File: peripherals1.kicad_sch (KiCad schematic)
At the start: 39 parts, among them Q1 Q_NMOS_GSD, SW3 SW_Push, SW4 SW_Push, SW5 SW_Push, SW6 SW_Push, SW7 SW_Push, SW8 SW_Push, U7 TSDP343xx

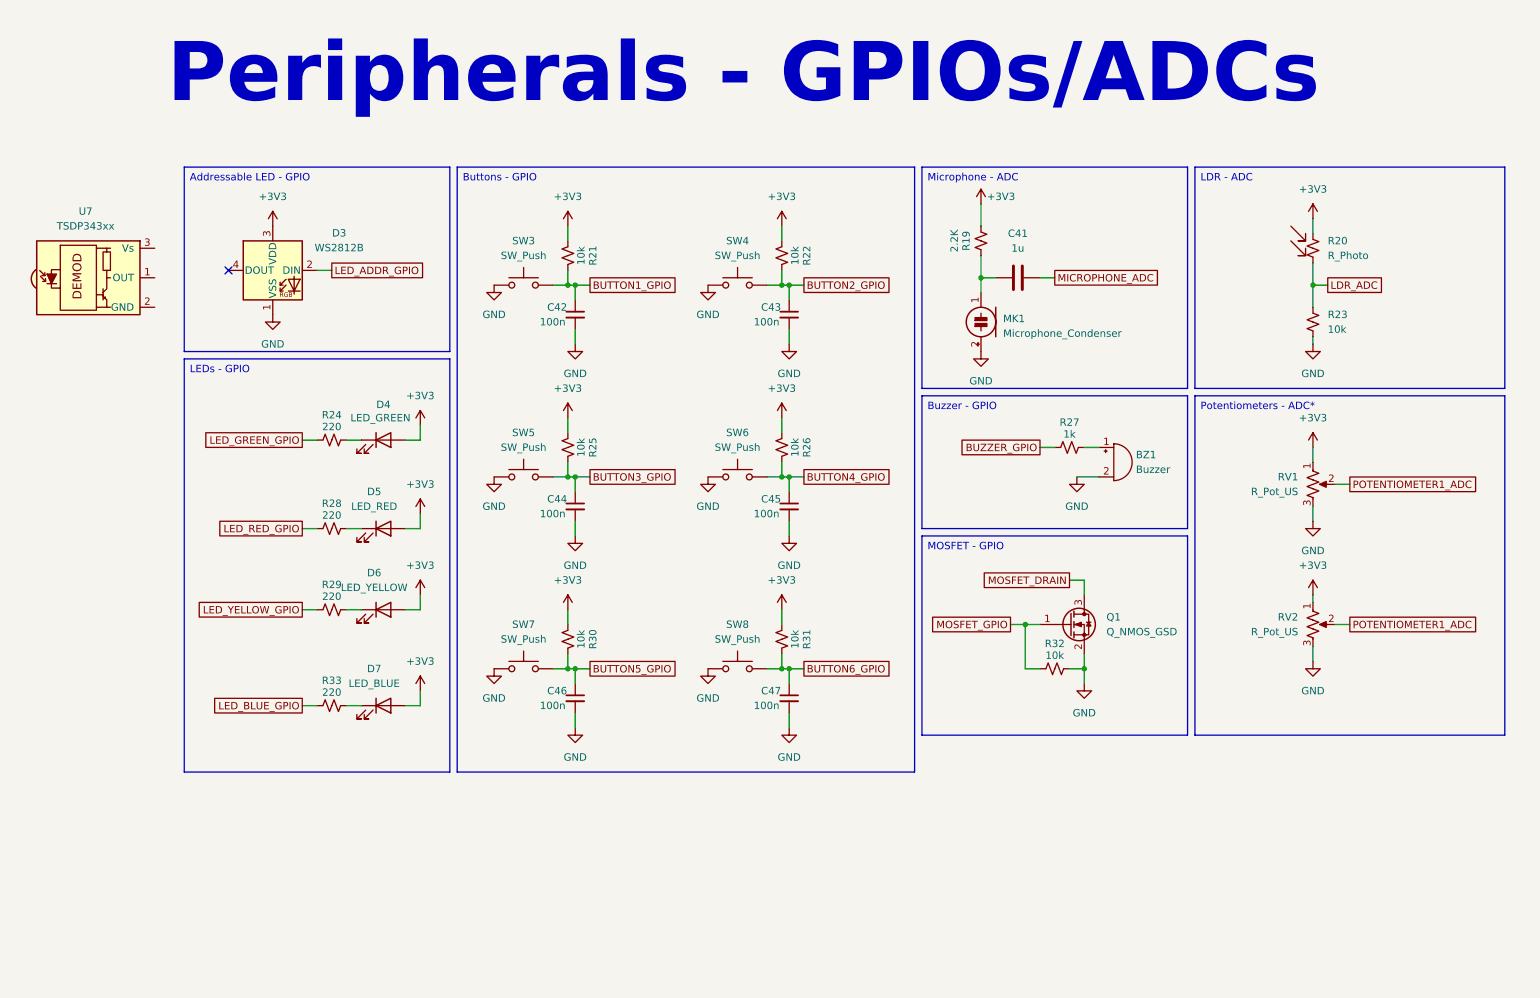
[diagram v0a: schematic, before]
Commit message: feat: adds IR components
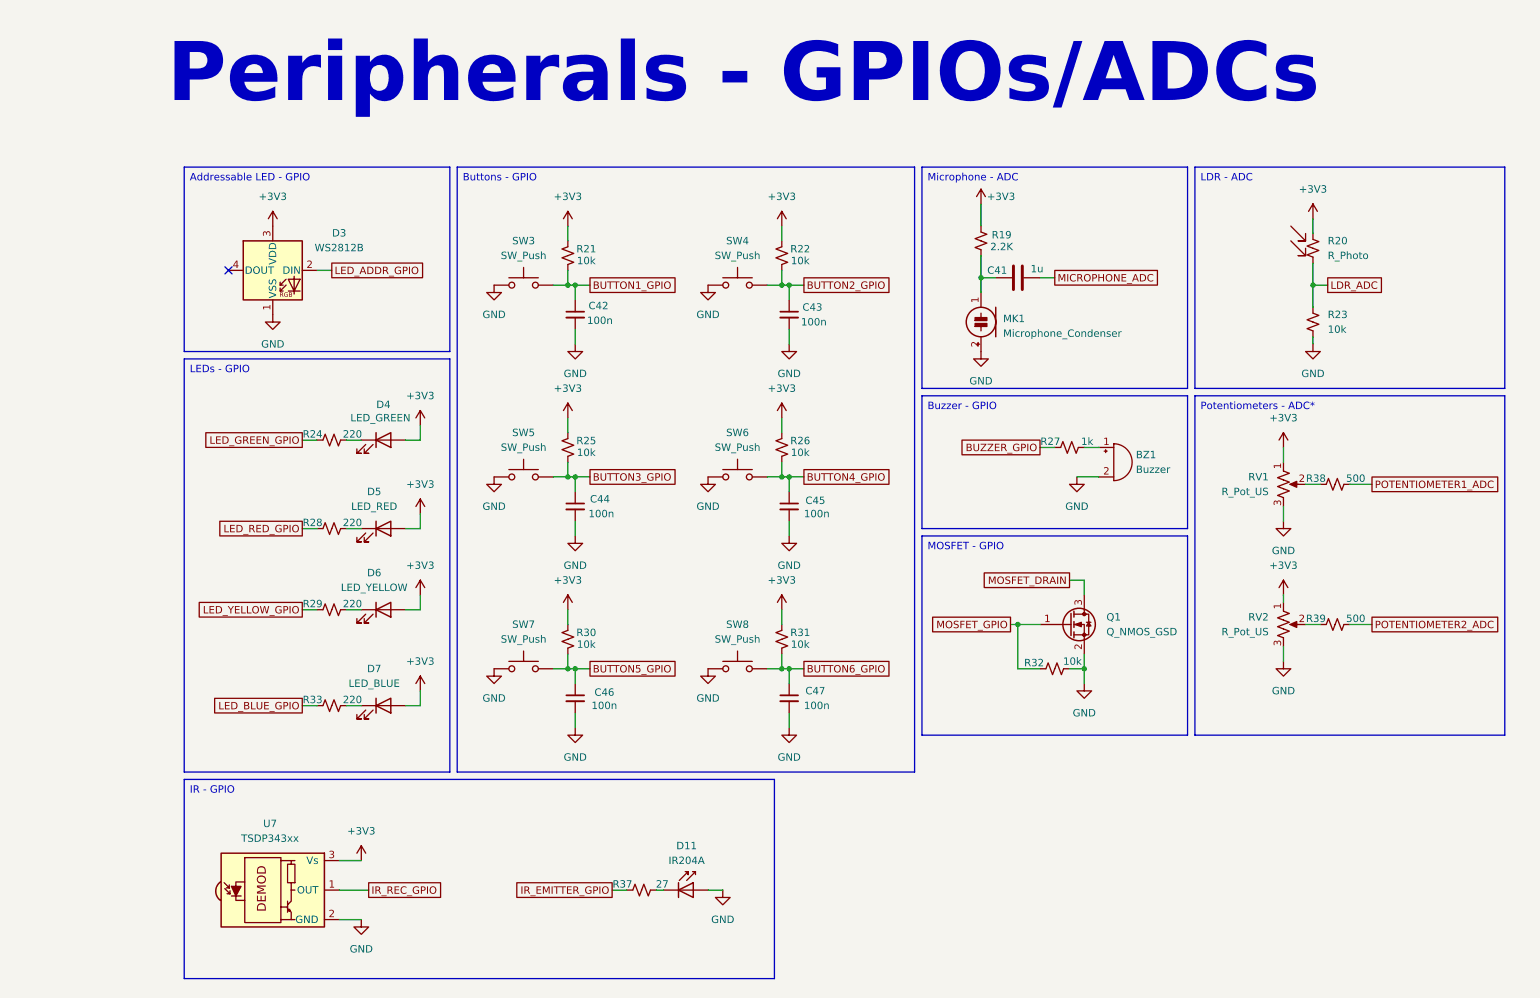
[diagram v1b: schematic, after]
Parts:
- added D11: IR204A, Diode_SMD:D_0603_1608Metric, symbol LED:IR204A
- added R37: 27, Resistor_SMD:R_0402_1005Metric, symbol Device:R_Small_US
- added R38, R39: 500, Resistor_SMD:R_0402_1005Metric, symbol Device:R_Small_US
- U7: MPN (none) -> TSDP34156
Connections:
- net +3V3: now also U7.3 (Vs)
- net GND: now also U7.2 (GND), D11.2 (A)
- net POTENTIOMETER1_ADC: now also R38.2; no longer RV1.2, RV2.2
- net IR_REC_GPIO: now reaches U7.1 (OUT)
- new net: R39.1, RV2.2
- new net: R38.1, RV1.2
- new net: D11.1 (K), R37.2
- new net IR_EMITTER_GPIO: R37.1
- new net POTENTIOMETER2_ADC: R39.2
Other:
- moved on the sheet: RV1, RV2, U7

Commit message: refac: moves circuits around
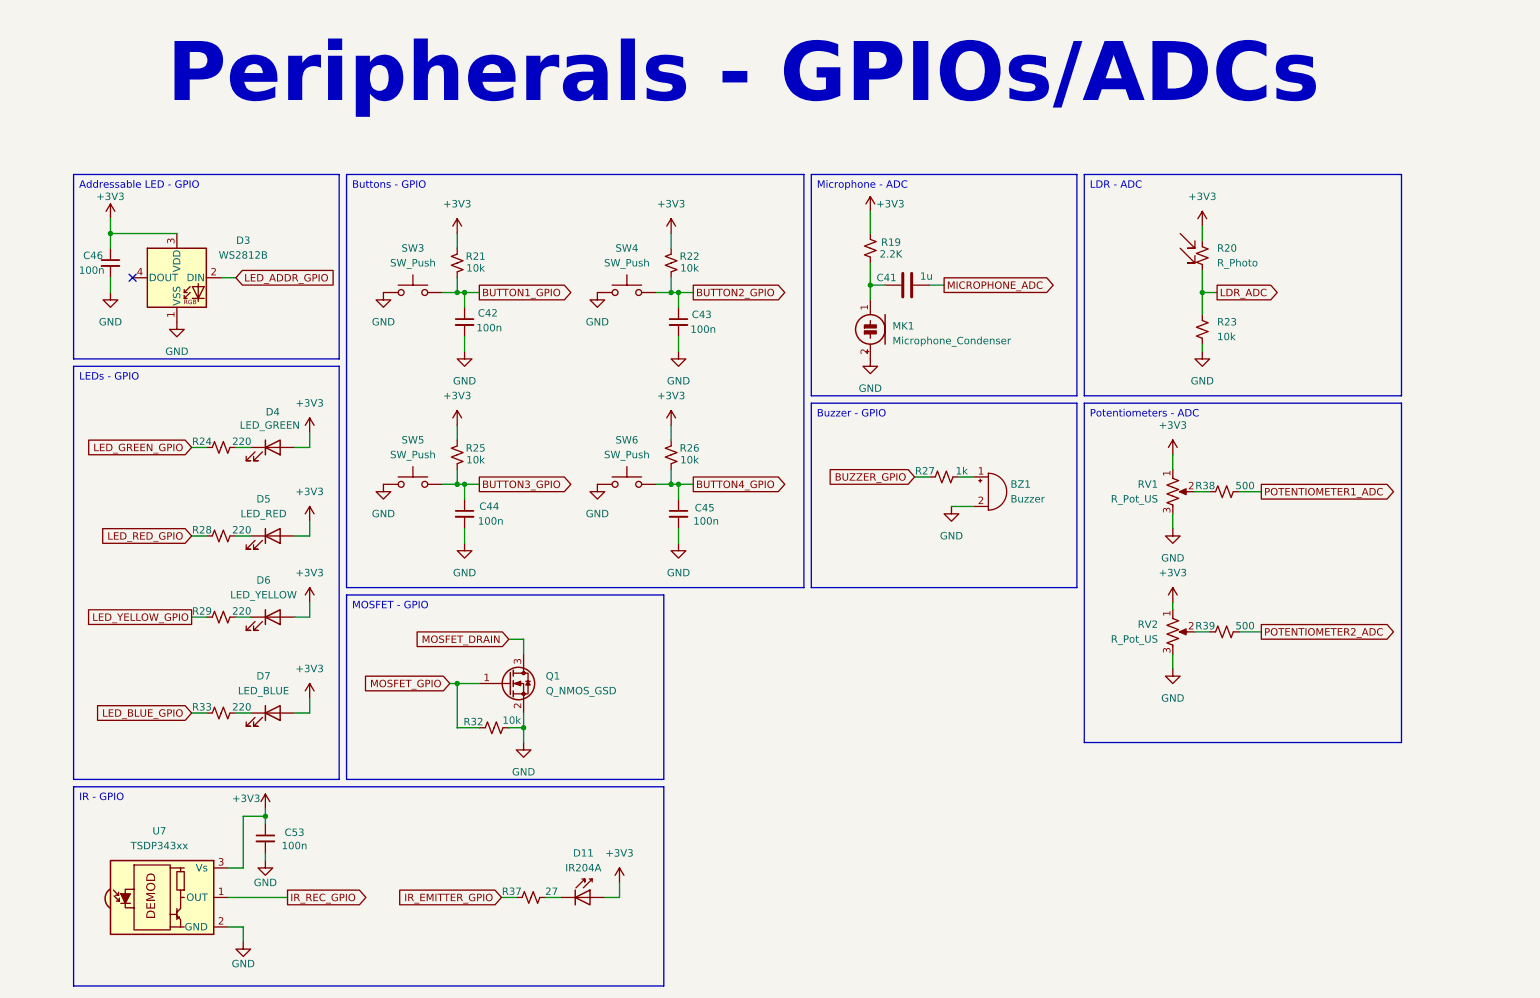
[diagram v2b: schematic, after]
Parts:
- removed C47: 100n, Capacitor_SMD:C_0402_1005Metric, symbol Device:C_Small
- removed R30, R31: 10k, Resistor_SMD:R_0402_1005Metric, symbol Device:R_Small_US
- removed SW7, SW8: SW_Push, symbol Switch:SW_Push
- added C53: 100n, Capacitor_SMD:C_0402_1005Metric, symbol Device:C_Small
- D4: footprint (none) -> LED_SMD:LED_0603_1608Metric; MPN LGR971-KN-1 -> LG Q976.01-MGNI-35-1
- D5, D6, D7: footprint (none) -> LED_SMD:LED_0603_1608Metric
- Q1: MPN DMN2600UFB-7 -> FDN327N
- RV1, RV2: footprint (none) -> Potentiometer_THT:Potentiometer_Vishay_148-149_Single_Horizontal
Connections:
- net BUTTON5_GPIO is gone; now on net +3V3: C46.1
- net +3V3: now also D11.2 (A), C53.1
- net GND: now also C53.2; no longer D11.2 (A)
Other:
- moved on the sheet: BZ1, C41, C42, C43, C44, C45, D11, D3, D4, D5, D6, D7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

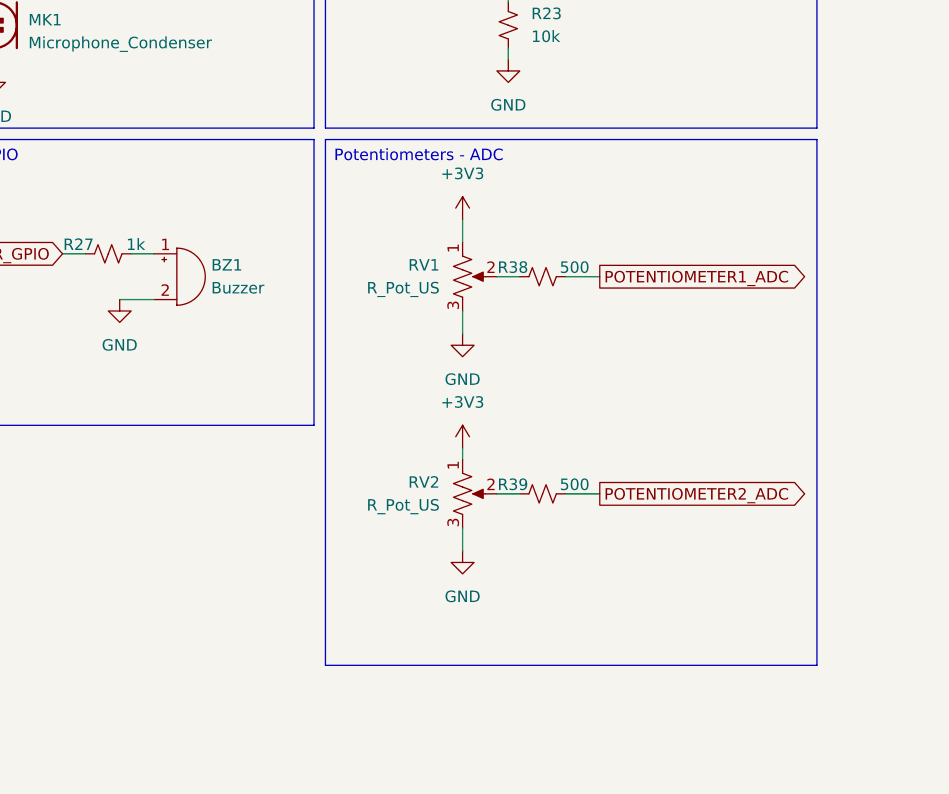
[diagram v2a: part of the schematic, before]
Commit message: feat: adds footprints to Peripherals1 sheet components
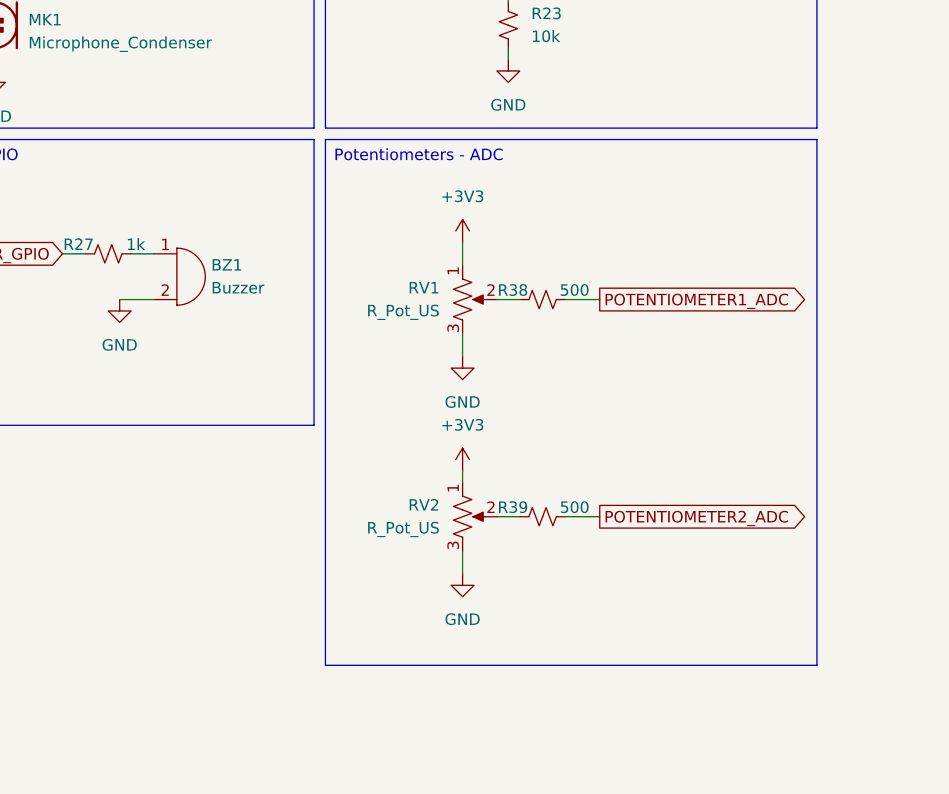
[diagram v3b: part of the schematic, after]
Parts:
- BZ1: footprint (none) -> Buzzer_Beeper:Buzzer_TDK_PS1240P02BT_D12.2mm_H6.5mm; MPN PKHPS0013E4000-A2 -> PS1440P02BT
- C41: footprint (none) -> Capacitor_SMD:C_0402_1005Metric
- D3: footprint (none) -> peripherals1:LED_FZ2812-5050
- MK1: footprint (none) -> peripherals1:CMEJ-0415_CUD
- Q1: footprint (none) -> Package_TO_SOT_SMD:SOT-23
- R20: footprint (none) -> OptoDevice:R_LDR_5.1x4.3mm_P3.4mm_Vertical
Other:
- moved on the sheet: R38, R39, RV1, RV2

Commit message: feat: adds button footprints in peripherals sheet
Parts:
- SW3, SW4, SW5, SW6: footprint (none) -> microcontroller:SMD Button
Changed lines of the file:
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@@
 			)
 		)
-		(property "Footprint" ""
+		(property "Footprint" "microcontroller:SMD Button"
 			(at 130.81 54.61 0)
 			(effects
@@
 			)
 		)
-		(property "Footprint" ""
+		(property "Footprint" "microcontroller:SMD Button"
 			(at 93.98 87.63 0)
 			(effects
@@
 			)
 		)
-		(property "Footprint" ""
+		(property "Footprint" "microcontroller:SMD Button"
 			(at 93.98 54.61 0)
 			(effects
@@
 			)
 		)
-		(property "Footprint" ""
+		(property "Footprint" "microcontroller:SMD Button"
 			(at 130.81 87.63 0)
 			(effects

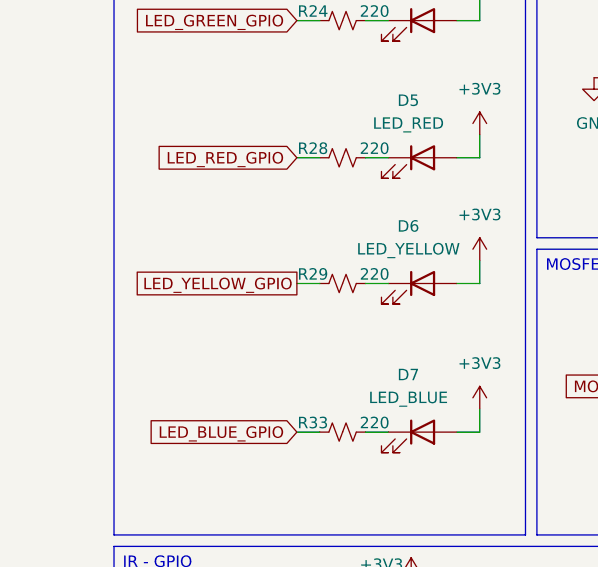
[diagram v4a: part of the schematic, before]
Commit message: feat: adds pin headers
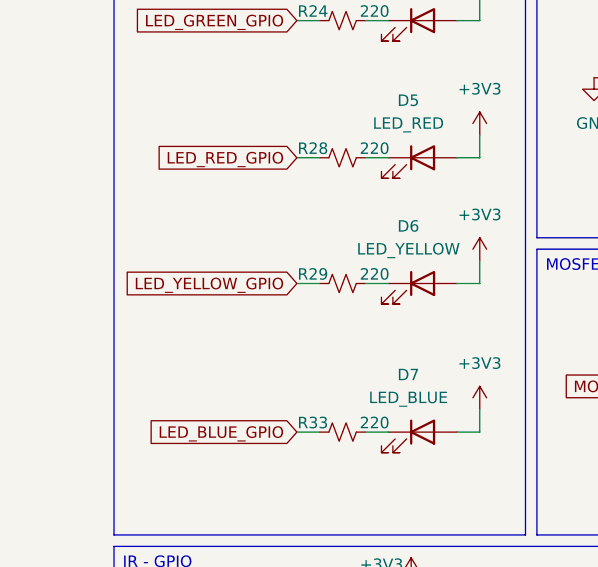
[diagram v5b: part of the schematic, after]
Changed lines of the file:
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@@
 	)
 	(global_label "LED_YELLOW_GPIO"
-		(shape passive)
+		(shape input)
 		(at 55.88 115.57 180)
 		(fields_autoplaced yes)
